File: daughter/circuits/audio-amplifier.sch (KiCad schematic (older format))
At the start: 22 parts, among them J10 AudioJack_3.5TRS, J8 AudioJack_3.5TRS, J9 Conn_01x05, U8 TDA7851F

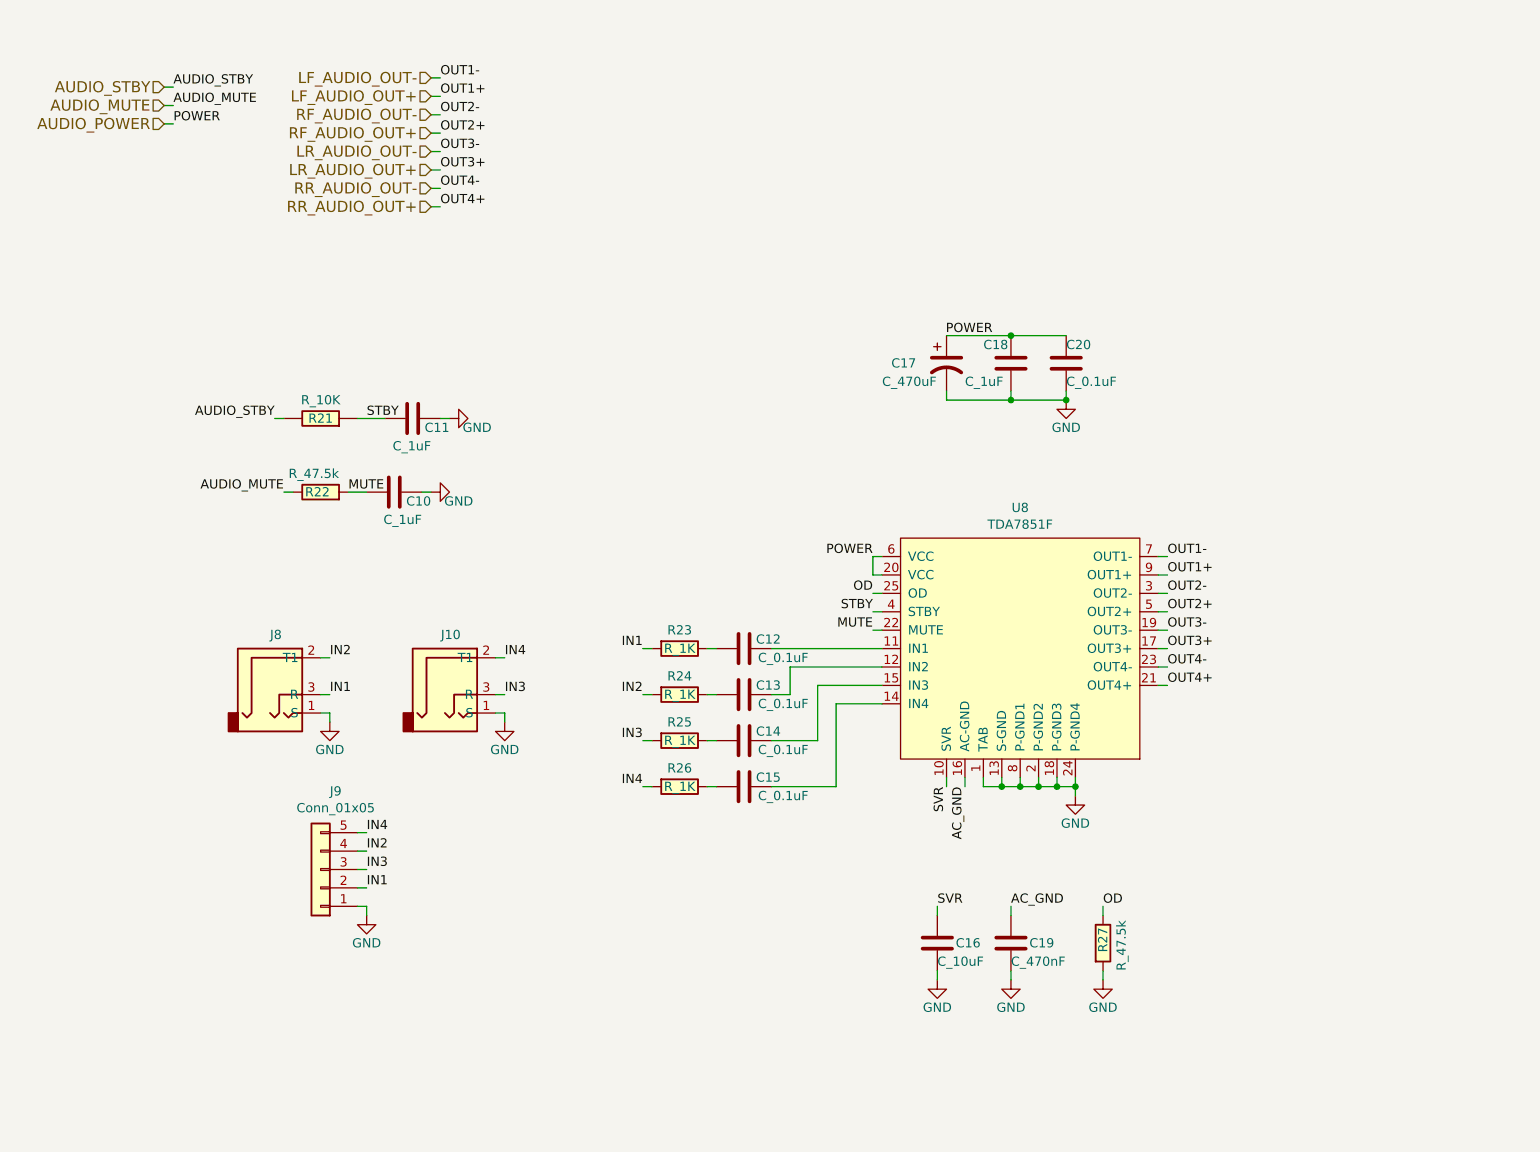
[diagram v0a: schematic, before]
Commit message: 0) Switched to h-bridge drivers for hvac 1) Connected ignition sense io 2) MCP config pins and reset 3) Fixed usb resistors 4) Fixed BJT footprint 5) Added car interface pcb for C6 Corvette
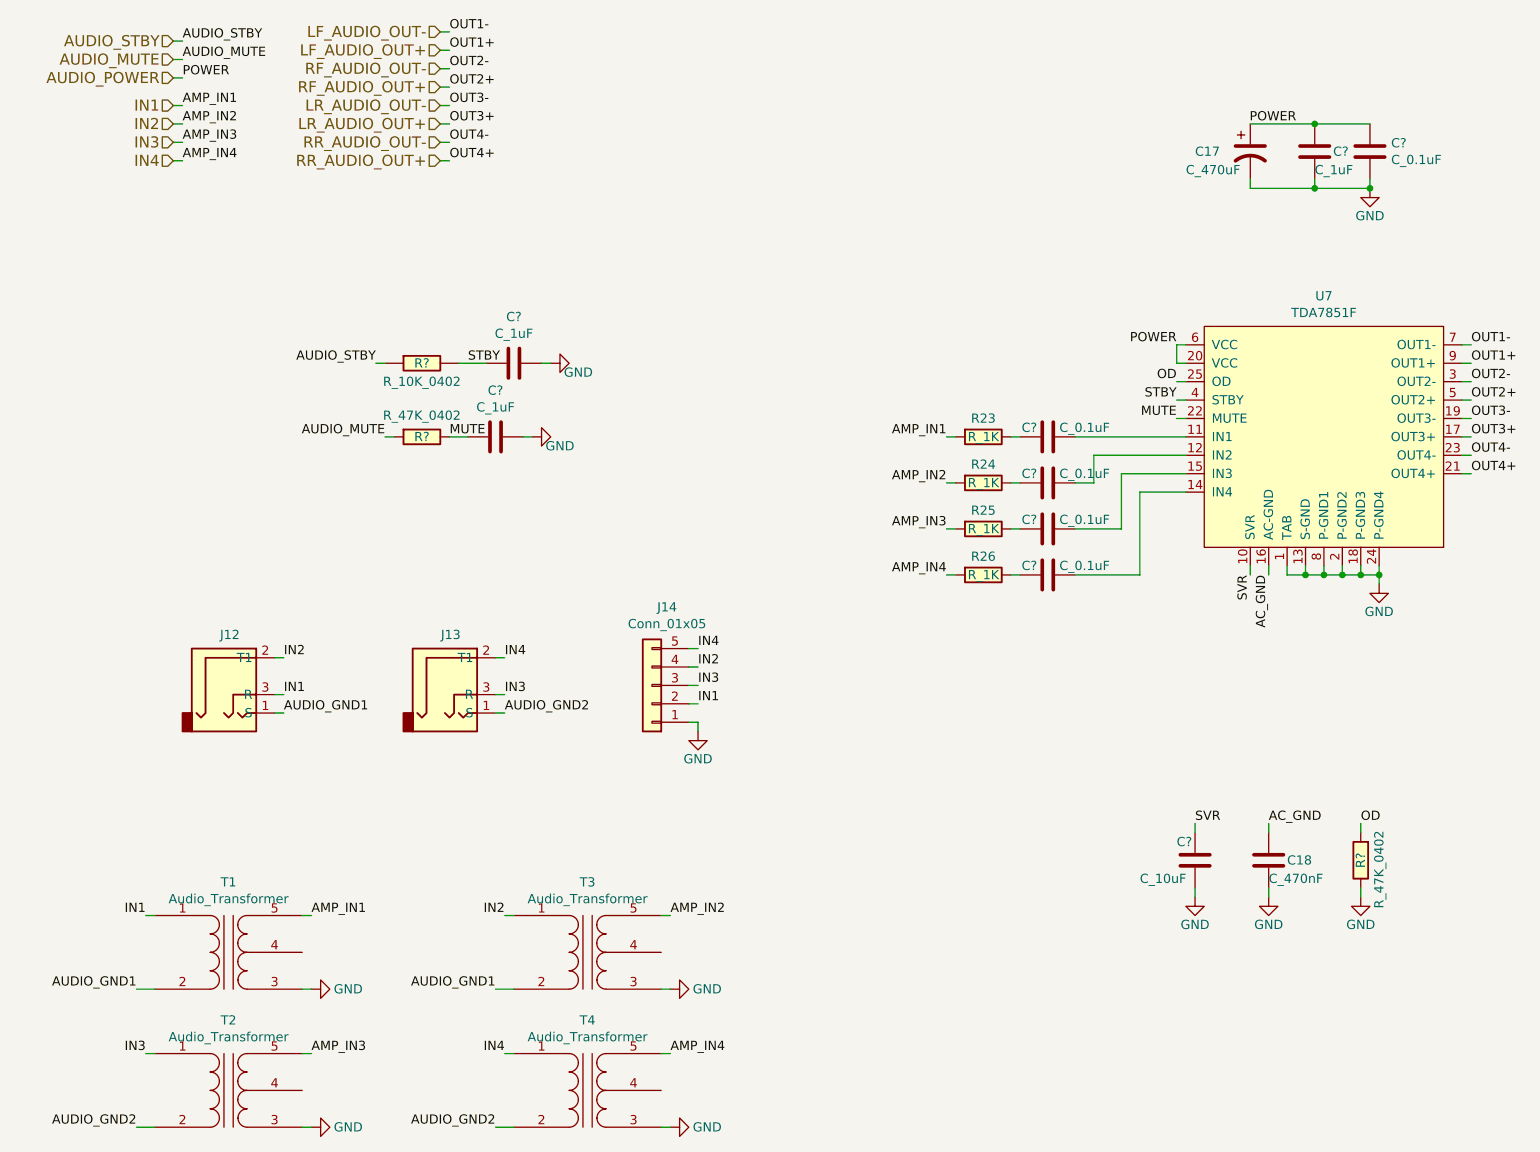
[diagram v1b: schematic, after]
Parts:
- removed C10, C11, C18: C_1uF, Capacitor_SMD:C_0603_1608Metric_Pad1.08x0.95mm_HandSolder, symbol open-dash-daughterboard-rescue:C_1uF-Open_Automation
- removed C12, C13, C14, C15, C20: C_0.1uF, Capacitor_SMD:C_0603_1608Metric_Pad1.08x0.95mm_HandSolder, symbol open-dash-daughterboard-rescue:C_0.1uF-Open_Automation
- removed C16: C_10uF, Capacitor_SMD:C_0603_1608Metric_Pad1.08x0.95mm_HandSolder, symbol open-dash-daughterboard-rescue:C_10uF-Open_Automation
- removed R21: R_10K, Resistor_SMD:R_0603_1608Metric_Pad0.98x0.95mm_HandSolder, symbol open-dash-daughterboard-rescue:R_10K-Open_Automation
- removed R22, R27: R_47.5k, Resistor_SMD:R_0603_1608Metric_Pad0.98x0.95mm_HandSolder, symbol open-dash-daughterboard-rescue:R_47.5k-Open_Automation
- added C? (x3): C_1uF, Capacitor_SMD:C_0402_1005Metric_Pad0.74x0.62mm_HandSolder, symbol Open_Automation:C_1uF
- added C? (x5): C_0.1uF, Capacitor_SMD:C_0402_1005Metric_Pad0.74x0.62mm_HandSolder, symbol Open_Automation:C_0.1uF
- added C?: C_10uF, Capacitor_SMD:C_0805_2012Metric_Pad1.18x1.45mm_HandSolder, symbol Open_Automation:C_10uF
- added R?: R_10K_0402, Resistor_SMD:R_0402_1005Metric_Pad0.72x0.64mm_HandSolder, symbol Open_Automation:R_10K_0402
- added R? (x2): R_47K_0402, Resistor_SMD:R_0402_1005Metric_Pad0.72x0.64mm_HandSolder, symbol Open_Automation:R_47K_0402
- added T1, T2, T3, T4: Audio_Transformer, Open_Automation:Audio_Transformer, symbol Open_Automation:Audio_Transformer
- renumbered C19 to C18, J8 to J12, J10 to J13, J9 to J14, U8 to U7
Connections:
- net AUDIO_MUTE: now also R?.2
- net AUDIO_POWER: now also C?.1, C?.2
- net AUDIO_STBY: now also R?.1
- net GND: now also C?.1, C?.1, C?.1, C?.2, C?.2, R?.1, T1.3 (SA), T2.3 (SA), T3.3 (SA), T4.3 (SA); no longer J12.1 (S), J13.1 (S)
- net IN1: now also T1.1 (AA), T1.5 (SB)
- net IN2: now also T3.1 (AA), T3.5 (SB)
- net IN3: now also T2.1 (AA), T2.5 (SB)
- net IN4: now also T4.1 (AA), T4.5 (SB)
- net MUTE: now also C?.2, R?.1
- net OD: now also R?.2
- net STBY: now also C?.2, R?.2
- net SVR: now also C?.1
- net at U7.11 (IN1): now also C?.1
- net at U7.12 (IN2): now also C?.1
- net at U7.14 (IN4): now also C?.1
- net at U7.15 (IN3): now also C?.1
- net at R23.1: now also C?.2
- net at R24.1: now also C?.2
- net at R25.1: now also C?.2
- net at R26.1: now also C?.2
- new net AUDIO_GND1: J12.1 (S), T1.2 (AB), T3.2 (AB)
- new net AUDIO_GND2: J13.1 (S), T2.2 (AB), T4.2 (AB)
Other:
- moved on the sheet: C17, C18, J12, J14, R23, R24, R25, R26, U7

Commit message: finished schematic, working on layout
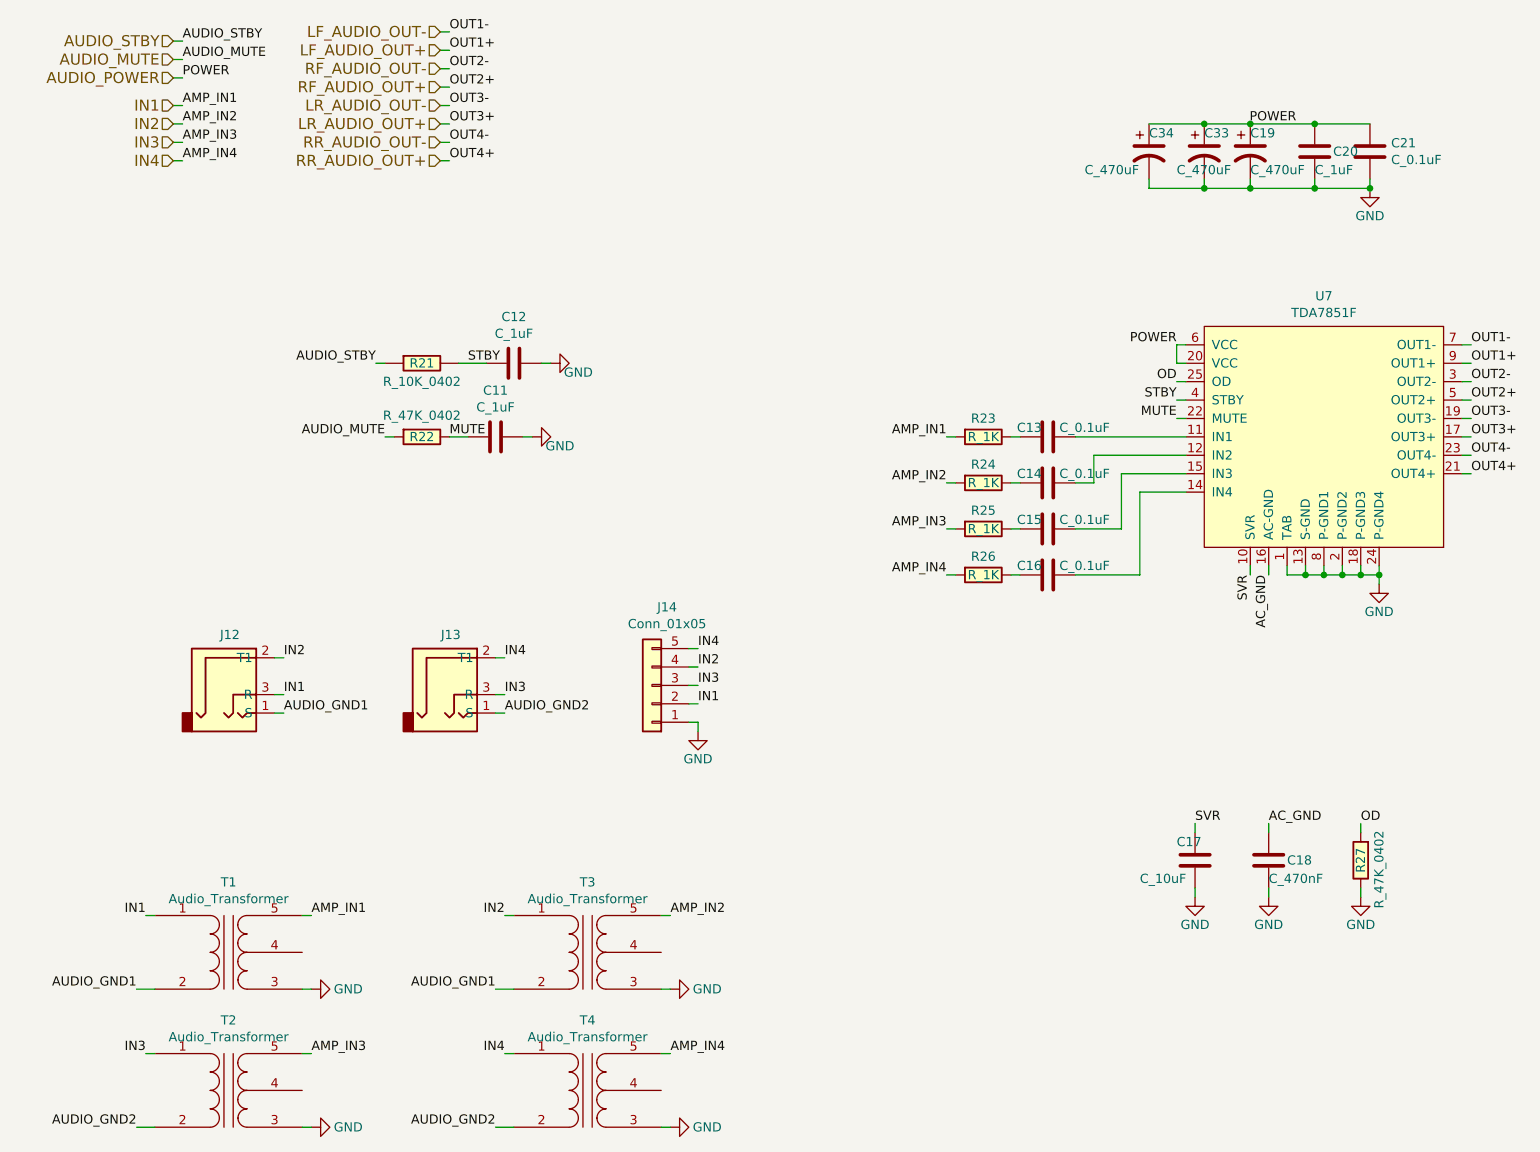
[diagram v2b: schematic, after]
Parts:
- removed C17: C_470uF, Capacitor_THT:CP_Radial_D8.0mm_P3.50mm, symbol open-dash-daughterboard-rescue:C_470uF-Open_Automation
- added C19, C33, C34: C_470uF, Capacitor_SMD:CP_Elec_10x10, symbol Open_Automation:C_470uF
- gave numbers to parts that had none: 12
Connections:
- net AUDIO_POWER: now also C19.1, C33.1, C34.1
- net GND: now also C19.2, C33.2, C34.2
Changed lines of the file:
@@
-$EndComp
-$Comp
-L open-dash-daughterboard-rescue:C_470uF-Open_Automation C17
-U 1 1 5D065E91
-P 7600 1650
-F 0 "C17" H 7300 1650 50  0000 L CNN
-F 1 "C_470uF" H 7250 1550 50  0000 L CNN
-F 2 "Capacitor_THT:CP_Radial_D8.0mm_P3.50mm" H 7600 1650 50  0001 C CNN
-F 3 "https://katalog.we-online.de/pbs/datasheet/860020474014.pdf" H 7600 1650 50  0001 C CNN
-F 4 " 860020474014" H 7600 1650 50  0001 C CNN "Part Number"
-	1    7600 1650
-	1    0    0    -1
 $EndComp
 $Comp
@@
 AMP_IN4
 $Comp
-L Open_Automation:R_10K_0402 R?
+L Open_Automation:R_10K_0402 R21
 U 1 1 6051433F
 P 3100 2800
-F 0 "R?" V 3100 2800 50  0000 C CNN
+F 0 "R21" V 3100 2800 50  0000 C CNN
 F 1 "R_10K_0402" V 3200 2800 50  0000 C CNN
 F 2 "Resistor_SMD:R_0402_1005Metric_Pad0.72x0.64mm_HandSolder" V 3030 2800 50  0001 C CNN
@@
 $EndComp
 $Comp
-L Open_Automation:C_1uF C?
+L Open_Automation:C_1uF C12
 U 1 1 60516623
 P 3600 2800
-F 0 "C?" V 3348 2800 50  0000 C CNN
+F 0 "C12" V 3348 2800 50  0000 C CNN
 F 1 "C_1uF" V 3439 2800 50  0000 C CNN
 F 2 "Capacitor_SMD:C_0402_1005Metric_Pad0.74x0.62mm_HandSolder" H 3700 3100 50  0001 C CNN
@@
 $EndComp
 $Comp
-L Open_Automation:C_1uF C?
+L Open_Automation:C_1uF C11
 U 1 1 60516BD4
 P 3500 3200
-F 0 "C?" V 3248 3200 50  0000 C CNN
+F 0 "C11" V 3248 3200 50  0000 C CNN
 F 1 "C_1uF" V 3339 3200 50  0000 C CNN
 F 2 "Capacitor_SMD:C_0402_1005Metric_Pad0.74x0.62mm_HandSolder" H 3600 3500 50  0001 C CNN
@@
 	7600 1500 7950 1500
 $Comp
-L Open_Automation:C_1uF C?
+L Open_Automation:C_1uF C20
 U 1 1 60517E72
 P 7950 1650
-F 0 "C?" H 7850 1650 50  0000 R CNN
+F 0 "C20" H 7850 1650 50  0000 R CNN
 F 1 "C_1uF" H 7950 1750 50  0000 R CNN
 F 2 "Capacitor_SMD:C_0402_1005Metric_Pad0.74x0.62mm_HandSolder" H 8050 1950 50  0001 C CNN
@@
 	7950 1500 8250 1500
 $Comp
-L Open_Automation:C_0.1uF C?
+L Open_Automation:C_0.1uF C21
 U 1 1 605193C1
 P 8250 1650
-F 0 "C?" H 8365 1696 50  0000 L CNN
+F 0 "C21" H 8365 1696 50  0000 L CNN
 F 1 "C_0.1uF" H 8365 1605 50  0000 L CNN
 F 2 "Capacitor_SMD:C_0402_1005Metric_Pad0.74x0.62mm_HandSolder" H 8350 1950 50  0001 C CNN
@@
 $EndComp
 $Comp
-L Open_Automation:C_10uF C?
+L Open_Automation:C_10uF C17
 U 1 1 6051CBF8
 P 7300 5500
-F 0 "C?" H 7200 5600 50  0000 L CNN
+F 0 "C17" H 7200 5600 50  0000 L CNN
 F 1 "C_10uF" H 7000 5400 50  0000 L CNN
 F 2 "Capacitor_SMD:C_0805_2012Metric_Pad1.18x1.45mm_HandSolder" H 7550 5950 50  0001 C CNN
@@
 $EndComp
 $Comp
-L Open_Automation:C_0.1uF C?
+L Open_Automation:C_0.1uF C13
 U 1 1 605275DE
 P 6500 3200
-F 0 "C?" V 6450 3100 50  0000 C CNN
+F 0 "C13" V 6450 3100 50  0000 C CNN
 F 1 "C_0.1uF" V 6450 3400 50  0000 C CNN
 F 2 "Capacitor_SMD:C_0402_1005Metric_Pad0.74x0.62mm_HandSolder" H 6600 3500 50  0001 C CNN
@@
 $EndComp
 $Comp
-L Open_Automation:C_0.1uF C?
+L Open_Automation:C_0.1uF C14
 U 1 1 6052A102
 P 6500 3450
-F 0 "C?" V 6450 3350 50  0000 C CNN
+F 0 "C14" V 6450 3350 50  0000 C CNN
 F 1 "C_0.1uF" V 6450 3650 50  0000 C CNN
 F 2 "Capacitor_SMD:C_0402_1005Metric_Pad0.74x0.62mm_HandSolder" H 6600 3750 50  0001 C CNN
@@
 $EndComp
 $Comp
-L Open_Automation:C_0.1uF C?
+L Open_Automation:C_0.1uF C15
 U 1 1 6052ABFB
 P 6500 3700
-F 0 "C?" V 6450 3600 50  0000 C CNN
+F 0 "C15" V 6450 3600 50  0000 C CNN
 F 1 "C_0.1uF" V 6450 3900 50  0000 C CNN
 F 2 "Capacitor_SMD:C_0402_1005Metric_Pad0.74x0.62mm_HandSolder" H 6600 4000 50  0001 C CNN
@@
 $EndComp
 $Comp
-L Open_Automation:C_0.1uF C?
+L Open_Automation:C_0.1uF C16
 U 1 1 6052AC07
 P 6500 3950
-F 0 "C?" V 6450 3850 50  0000 C CNN
+F 0 "C16" V 6450 3850 50  0000 C CNN
 F 1 "C_0.1uF" V 6450 4150 50  0000 C CNN
 F 2 "Capacitor_SMD:C_0402_1005Metric_Pad0.74x0.62mm_HandSolder" H 6600 4250 50  0001 C CNN
@@
 $EndComp
 $Comp
-L Open_Automation:R_47K_0402 R?
+L Open_Automation:R_47K_0402 R22
 U 1 1 6053A2D6
 P 3100 3200
-F 0 "R?" V 3100 3200 50  0000 C CNN
+F 0 "R22" V 3100 3200 50  0000 C CNN
 F 1 "R_47K_0402" V 2984 3200 50  0000 C CNN
 F 2 "Resistor_SMD:R_0402_1005Metric_Pad0.72x0.64mm_HandSolder" V 3030 3200 50  0001 C CNN
@@
 $EndComp
 $Comp
-L Open_Automation:R_47K_0402 R?
+L Open_Automation:R_47K_0402 R27
 U 1 1 6053E9DA
 P 8200 5500
-F 0 "R?" V 8200 5500 50  0000 C CNN
+F 0 "R27" V 8200 5500 50  0000 C CNN
 F 1 "R_47K_0402" V 8100 5550 50  0000 C CNN
 F 2 "Resistor_SMD:R_0402_1005Metric_Pad0.72x0.64mm_HandSolder" V 8130 5500 50  0001 C CNN
@@
 	-1   0    0    1
 $EndComp
+$Comp
+L Open_Automation:C_470uF C19
+U 1 1 604E0E85
+P 7600 1650
+F 0 "C19" H 7600 1750 50  0000 L CNN
+F 1 "C_470uF" H 7600 1550 50  0000 L CNN
+F 2 "Capacitor_SMD:CP_Elec_10x10" H 7600 1650 50  0001 C CNN
+F 3 "https://datasheet.lcsc.com/szlcsc/1809192324_Honor-Elec-RVT1V471M1010_C3350.pdf" H 7600 1650 50  0001 C CNN
+F 4 "RVT1V471M1010" H 7600 1650 50  0001 C CNN "Part Number"
+F 5 "C3350" H 7600 1650 50  0001 C CNN "LCSC"
+	1    7600 1650
+	1    0    0    -1
+$EndComp
+$Comp
+L Open_Automation:C_470uF C33
+U 1 1 61FE455E
+P 7350 1650
+F 0 "C33" H 7350 1750 50  0000 L CNN
+F 1 "C_470uF" H 7200 1550 50  0000 L CNN
+F 2 "Capacitor_SMD:CP_Elec_10x10" H 7350 1650 50  0001 C CNN
+F 3 "https://datasheet.lcsc.com/szlcsc/1809192324_Honor-Elec-RVT1V471M1010_C3350.pdf" H 7350 1650 50  0001 C CNN
+F 4 "RVT1V471M1010" H 7350 1650 50  0001 C CNN "Part Number"
+F 5 "C3350" H 7350 1650 50  0001 C CNN "LCSC"
+	1    7350 1650
+	1    0    0    -1
+$EndComp
+Wire Wire Line
+	7350 1800 7350 1850
+Wire Wire Line
+	7350 1850 7600 1850
+Connection ~ 7600 1850
+Wire Wire Line
+	7350 1500 7600 1500
+Connection ~ 7600 1500
+$Comp
+L Open_Automation:C_470uF C34
+U 1 1 61FF2E59
+P 7050 1650
+F 0 "C34" H 7050 1750 50  0000 L CNN
+F 1 "C_470uF" H 6700 1550 50  0000 L CNN
+F 2 "Capacitor_SMD:CP_Elec_10x10" H 7050 1650 50  0001 C CNN
+F 3 "https://datasheet.lcsc.com/szlcsc/1809192324_Honor-Elec-RVT1V471M1010_C3350.pdf" H 7050 1650 50  0001 C CNN
+F 4 "RVT1V471M1010" H 7050 1650 50  0001 C CNN "Part Number"
+F 5 "C3350" H 7050 1650 50  0001 C CNN "LCSC"
+	1    7050 1650
+	1    0    0    -1
+$EndComp
+Wire Wire Line
+	7050 1800 7050 1850
+Wire Wire Line
+	7050 1850 7350 1850
+Connection ~ 7350 1850
+Wire Wire Line
+	7050 1500 7350 1500
+Connection ~ 7350 1500
 $EndSCHEMATC

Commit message: finished layout
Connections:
- net IN1: no longer R23.2, T1.5 (SB)
- net IN2: no longer R24.2, T3.5 (SB)
- net IN3: no longer R25.2, T2.5 (SB)
- net IN4: no longer R26.2, T4.5 (SB)
- new net AMP_IN1: R23.2, T1.5 (SB)
- new net AMP_IN2: R24.2, T3.5 (SB)
- new net AMP_IN3: R25.2, T2.5 (SB)
- new net AMP_IN4: R26.2, T4.5 (SB)
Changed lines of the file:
@@
 Text Label 5950 3700 2    50   ~ 0
 AMP_IN3
-Text Label 5950 3950 2    50   ~ 0
-AMP_IN4
 Text Label 3350 2800 0    50   ~ 0
 STBY
@@
 $EndComp
 Text HLabel 1750 1500 0    60   Input ~ 0
-IN2
+AMP_IN2
 Text HLabel 1750 1700 0    60   Input ~ 0
-IN4
+AMP_IN4
 Text HLabel 1750 1600 0    60   Input ~ 0
-IN3
+AMP_IN3
 Text HLabel 1750 1400 0    60   Input ~ 0
-IN1
+AMP_IN1
 Wire Wire Line
 	1800 1700 1750 1700
@@
 Wire Wire Line
 	4450 6950 4400 6950
-Text Label 4450 6550 0    50   ~ 0
-AMP_IN4
-Wire Wire Line
-	4450 6550 4400 6550
 Text Label 1550 6200 2    50   ~ 0
 AUDIO_GND1
@@
 	7050 1500 7350 1500
 Connection ~ 7350 1500
+Wire Wire Line
+	4450 6550 4400 6550
+Text Label 5950 3950 2    50   ~ 0
+AMP_IN4
+Text Label 4450 6550 0    50   ~ 0
+AMP_IN4
 $EndSCHEMATC
